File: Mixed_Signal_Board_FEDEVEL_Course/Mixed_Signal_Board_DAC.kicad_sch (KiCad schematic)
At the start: 17 parts, among them J400 031-5640-1010, U400 DAC7563SDGSR, U401 MCP6001T-E/OT

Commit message: Handle the connections between sheets
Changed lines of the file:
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@@
 		)
 	)
-	(global_label "SPI2_SCK"
+	(hierarchical_label "SPI2_NSS"
 		(shape input)
-		(at 58.42 104.14 180)
-		(fields_autoplaced yes)
+		(at 58.42 107.95 180)
 		(effects
 			(font
@@
 			(justify right)
 		)
-		(property "Intersheetrefs" "${INTERSHEET_REFS}"
-			(at 46.4239 104.14 0)
-			(hide yes)
-			(show_name no)
-			(do_not_autoplace no)
-			(effects
-				(font
-					(size 1.27 1.27)
-				)
-				(justify right)
-			)
-		)
 	)
-	(global_label "DAC_NLDAC"
+	(hierarchical_label "DAC_NCLR"
 		(shape input)
-		(at 58.42 115.57 180)
-		(fields_autoplaced yes)
+		(at 58.42 111.76 180)
 		(effects
 			(font
@@
 			(justify right)
 		)
-		(property "Intersheetrefs" "${INTERSHEET_REFS}"
-			(at 44.8514 115.57 0)
-			(hide yes)
-			(show_name no)
-			(do_not_autoplace no)
-			(effects
-				(font
-					(size 1.27 1.27)
-				)
-				(justify right)
-			)
-		)
 	)
-	(global_label "DAC_NCLR"
+	(hierarchical_label "SPI2_MOSI"
 		(shape input)
-		(at 58.42 111.76 180)
-		(fields_autoplaced yes)
+		(at 58.42 100.33 180)
 		(effects
 			(font
@@
 			(justify right)
 		)
-		(property "Intersheetrefs" "${INTERSHEET_REFS}"
-			(at 45.94 111.76 0)
-			(hide yes)
-			(show_name no)
-			(do_not_autoplace no)
-			(effects
-				(font
-					(size 1.27 1.27)
-				)
-				(justify right)
-			)
-		)
 	)
-	(global_label "SPI2_MOSI"
+	(hierarchical_label "SPI2_SCK"
 		(shape input)
-		(at 58.42 100.33 180)
-		(fields_autoplaced yes)
+		(at 58.42 104.14 180)
 		(effects
 			(font
@@
 			(justify right)
 		)
-		(property "Intersheetrefs" "${INTERSHEET_REFS}"
-			(at 46.2382 100.2506 0)
-			(hide yes)
-			(show_name no)
-			(do_not_autoplace no)
-			(effects
-				(font
-					(size 1.27 1.27)
-				)
-				(justify right)
-			)
-		)
 	)
-	(global_label "SPI2_NSS"
+	(hierarchical_label "DAC_NLDAC"
 		(shape input)
-		(at 58.42 107.95 180)
-		(fields_autoplaced yes)
+		(at 58.42 115.57 180)
 		(effects
 			(font
@@
 			(justify right)
 		)
-		(property "Intersheetrefs" "${INTERSHEET_REFS}"
-			(at 46.4239 107.95 0)
-			(hide yes)
-			(show_name no)
-			(do_not_autoplace no)
-			(effects
-				(font
-					(size 1.27 1.27)
-				)
-				(justify right)
-			)
-		)
 	)

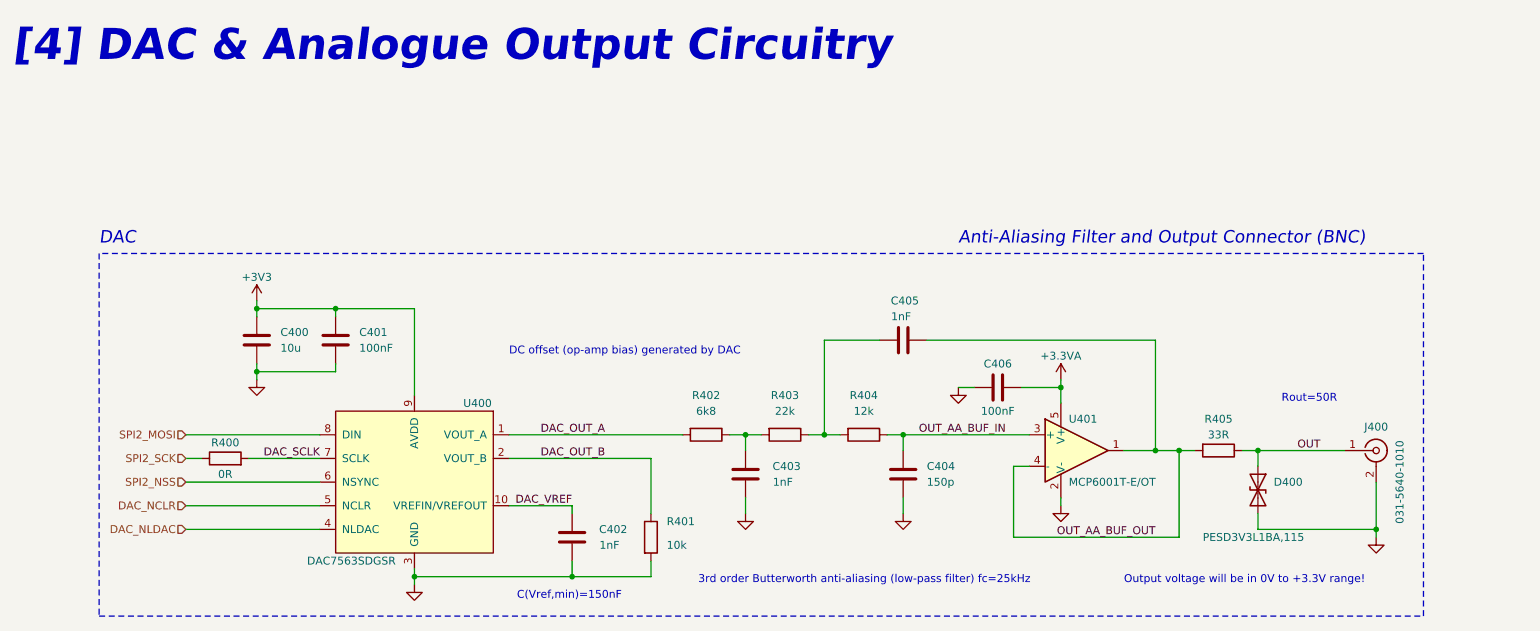
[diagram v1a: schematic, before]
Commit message: Solve the errors of sch after running the DRC
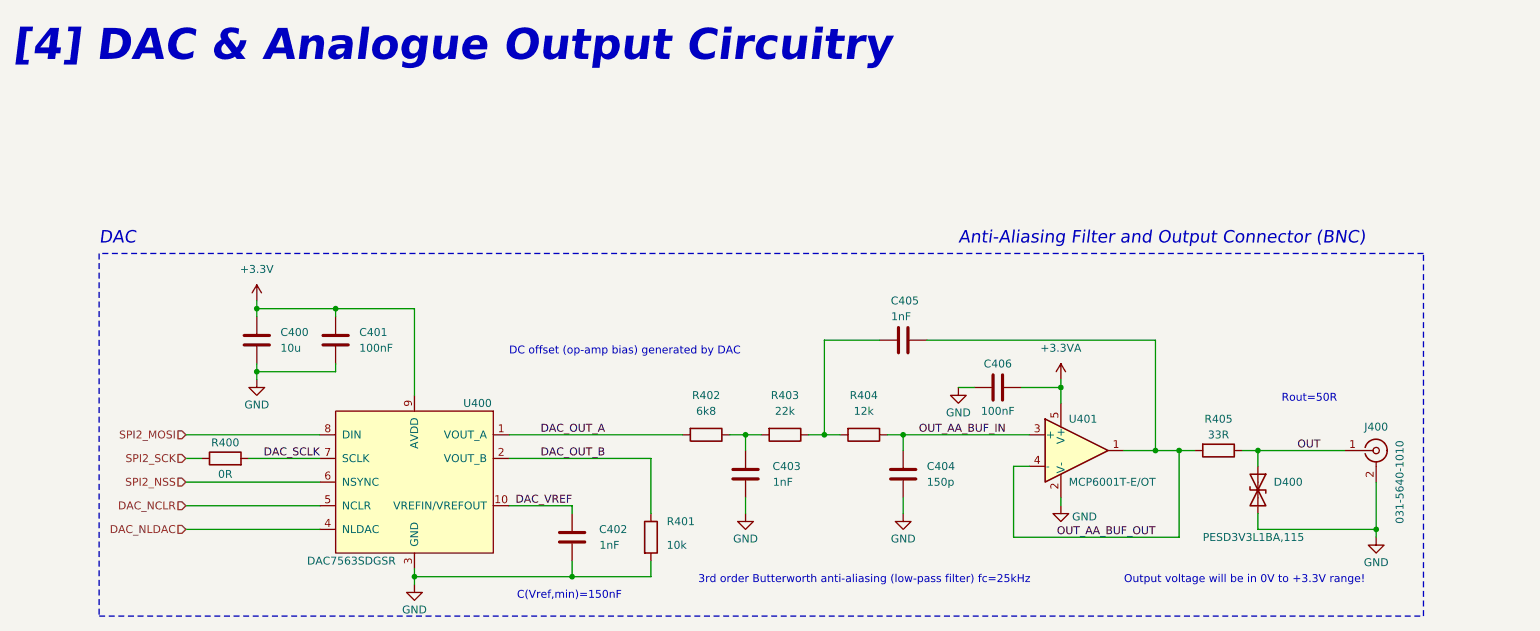
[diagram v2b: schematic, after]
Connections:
- net +3V3 renamed +3.3V

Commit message: Solve all warnings of the project
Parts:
- U400: symbol PhilsLab-KiCad-Symbols:DAC7563SDGSR -> PESD3V3L1BA,115:DAC7563SDGSR
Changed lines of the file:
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@@
 	)
 	(symbol
-		(lib_id "PhilsLab-KiCad-Symbols:DAC7563SDGSR")
+		(lib_id "PESD3V3L1BA,115:DAC7563SDGSR")
 		(at 95.25 107.95 0)
 		(mirror y)
